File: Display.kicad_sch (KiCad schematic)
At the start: 6 parts, among them J3 Conn_01x30_Pin, U1 rv1126/rv1109

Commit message: updated LCSC selection of capacitors
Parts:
- J3: footprint (none) -> Connector_FFC-FPC:Hirose_FH12-30S-0.5SH_1x30-1MP_P0.50mm_Horizontal
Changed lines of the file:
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@@
       (effects (font (size 1.27 1.27)) (justify right))
     )
-    (property "Footprint" "" (at 226.06 60.96 0)
+    (property "Footprint" "Connector_FFC-FPC:Hirose_FH12-30S-0.5SH_1x30-1MP_P0.50mm_Horizontal" (at 226.06 60.96 0)
       (effects (font (size 1.27 1.27)) hide)
     )

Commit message: layout SoC Power and DDR capacitors
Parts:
- C57: LCSC C76934 -> C76928; Model GRM033R61A104KE15D -> GRM033R60J104KE19D
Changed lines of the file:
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@@
       (effects (font (size 1.27 1.27)) hide)
     )
-    (property "Description" "容值: 100nF 精度: ±10% 额定电压: 10V 材质(温度系数): X5R 材质:X5R" (at 228.6 149.86 0)
-      (effects (font (size 1.27 1.27)) hide)
-    )
-    (property "LCSC" "C76934" (at 228.6 149.86 0)
-      (effects (font (size 1.27 1.27)) hide)
-    )
-    (property "Model" "GRM033R61A104KE15D" (at 228.6 149.86 0)
+    (property "Description" "容值: 100nF 精度: ±10% 额定电压: 6.3V 材质(温度系数): X5R 材质:X5R" (at 228.6 149.86 0)
+      (effects (font (size 1.27 1.27)) hide)
+    )
+    (property "LCSC" "C76928" (at 228.6 149.86 0)
+      (effects (font (size 1.27 1.27)) hide)
+    )
+    (property "Model" "GRM033R60J104KE19D" (at 228.6 149.86 0)
       (effects (font (size 1.27 1.27)) hide)
     )
@@
       (effects (font (size 1.27 1.27)) hide)
     )
-    (property "Description" "容值: 100nF 精度: ±10% 额定电压: 10V 材质(温度系数): X5R 材质:X5R" (at 184.15 148.59 0)
-      (effects (font (size 1.27 1.27)) hide)
-    )
-    (property "LCSC" "C76934" (at 184.15 148.59 0)
-      (effects (font (size 1.27 1.27)) hide)
-    )
-    (property "Model" "GRM033R61A104KE15D" (at 184.15 148.59 0)
-      (effects (font (size 1.27 1.27)) hide)
-    )
+    (property "Description" "容值: 100nF 精度: ±10% 额定电压: 6.3V 材质(温度系数): X5R 材质:X5R" (at 184.15 148.59 0)
+      (effects (font (size 1.27 1.27)) hide)
+    )
+    (property "LCSC" "C76928" (at 184.15 148.59 0)
+      (effects (font (size 1.27 1.27)) hide)
+    )
+    (property "Model" "GRM033R60J104KE19D" (at 184.15 148.59 0)
+      (effects (font (size 1.27 1.27)) hide)
+    )

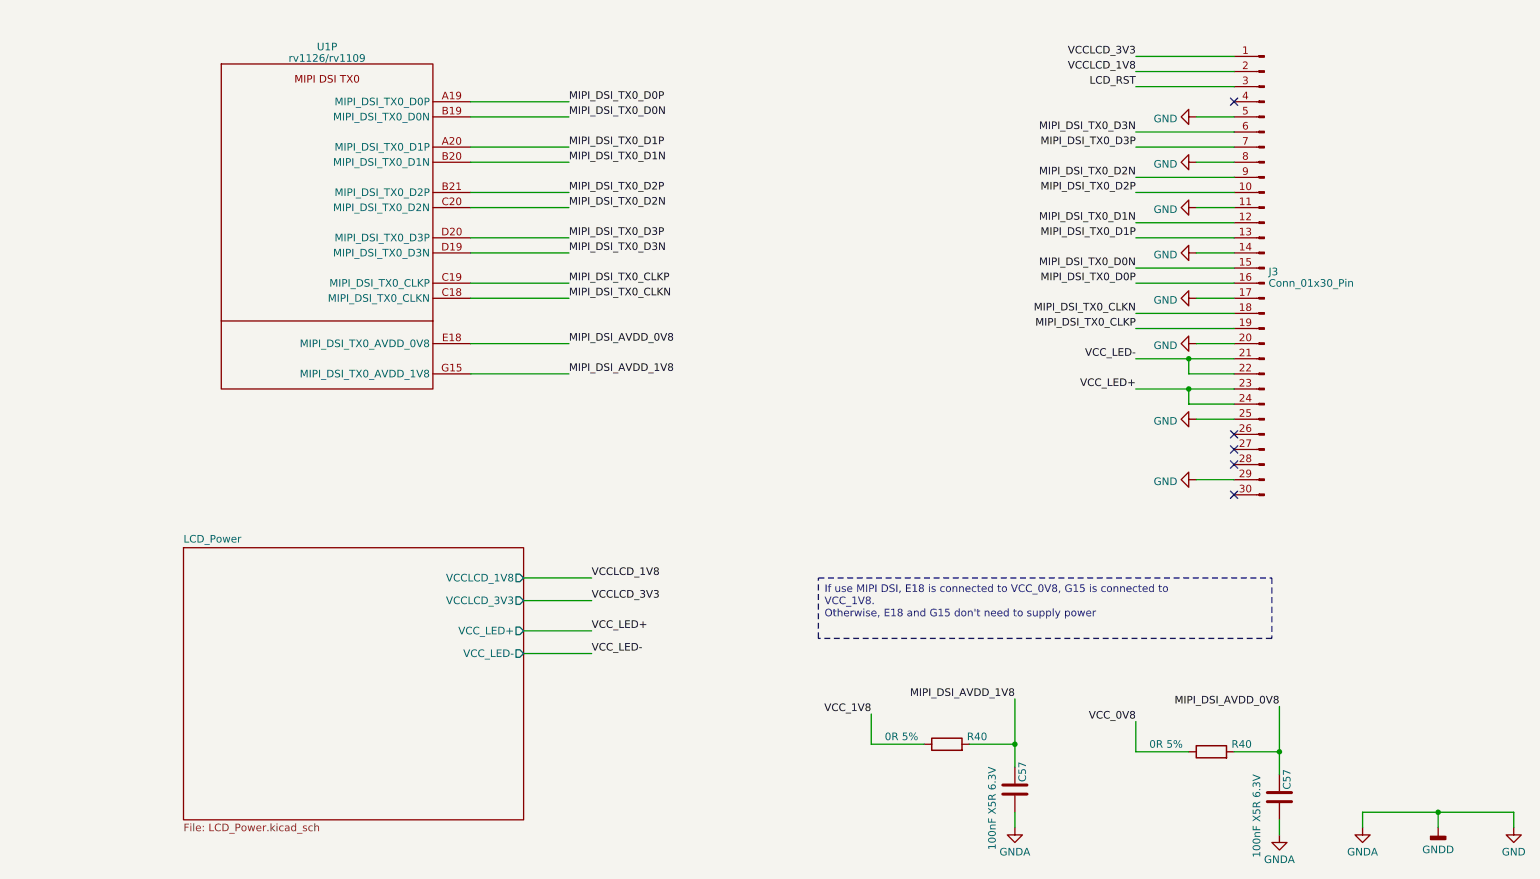
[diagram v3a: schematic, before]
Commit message: fix some ERCs
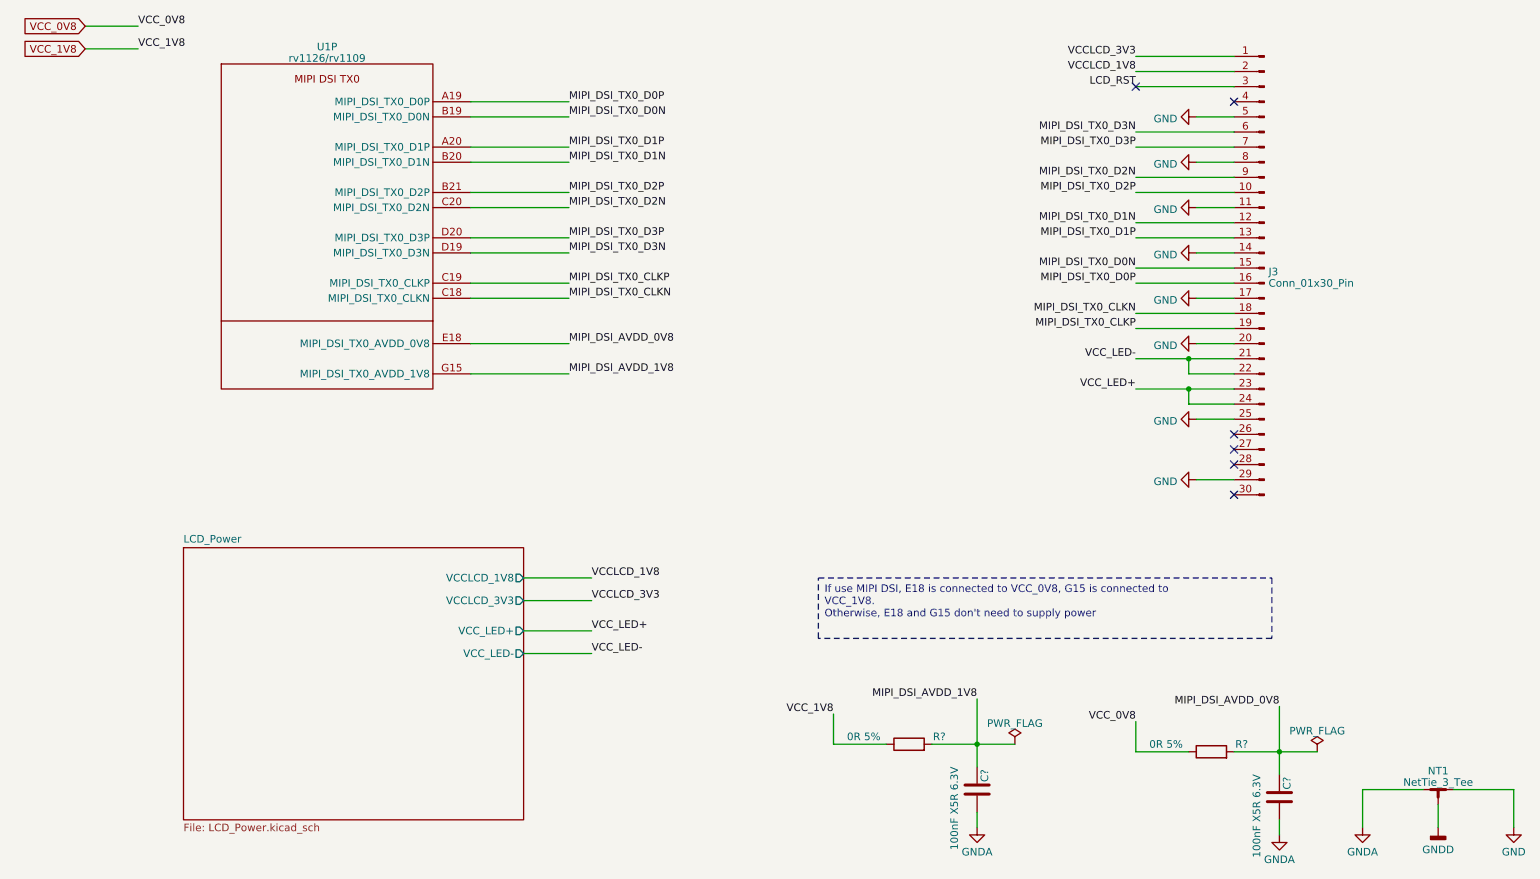
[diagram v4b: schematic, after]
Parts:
- added NT1: NetTie_3_Tee, symbol Device:NetTie_3_Tee
- renumbered C57 to C?, R40 to R?
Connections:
- net GND: now also NT1.2; no longer C?.2, C?.2
- new net GNDA: C?.2, C?.2, NT1.1
- new net GNDD: NT1.3
- no-connect marks 5 -> 6
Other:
- moved on the sheet: C?, R?

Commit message: fix ERC
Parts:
- J3: now not fitted; now left out of the parts list
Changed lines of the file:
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@@
     (pin "E20")
-    (pin "F19")
     (pin "F19")
     (pin "F20")
@@
   )
   (symbol (lib_id "Connector:Conn_01x30_Pin") (at 226.06 60.96 0) (mirror y) (unit 1)
-    (in_bom yes) (on_board yes) (dnp no) (fields_autoplaced)
+    (in_bom no) (on_board no) (dnp yes) (fields_autoplaced)
     (property "Reference" "J3" (at 226.7712 61.5863 0)
       (effects (font (size 1.27 1.27)) (justify right))

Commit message: updated symbols
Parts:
- removed C? (x2): 100nF X5R 6.3V, Capacitor_SMD:C_0201_0603Metric, symbol Device:C
- removed J3: Conn_01x30_Pin, Connector_FFC-FPC:Hirose_FH12-30S-0.5SH_1x30-1MP_P0.50mm_Horizontal, symbol Connector:Conn_01x30_Pin
- removed NT1: NetTie_3_Tee, symbol Device:NetTie_3_Tee
- removed R? (x2): 0R 5%, Resistor_SMD:R_0402_1005Metric, symbol Device:R
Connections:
- no-connect marks 6 -> 12
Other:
- removed sheet LCD_Power

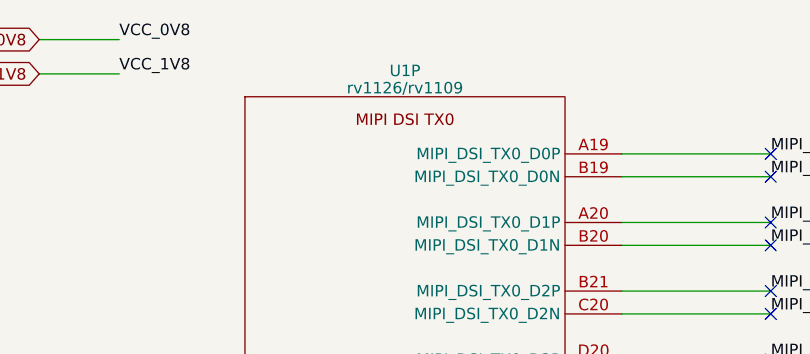
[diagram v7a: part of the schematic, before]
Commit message: added OSC, updated annotations
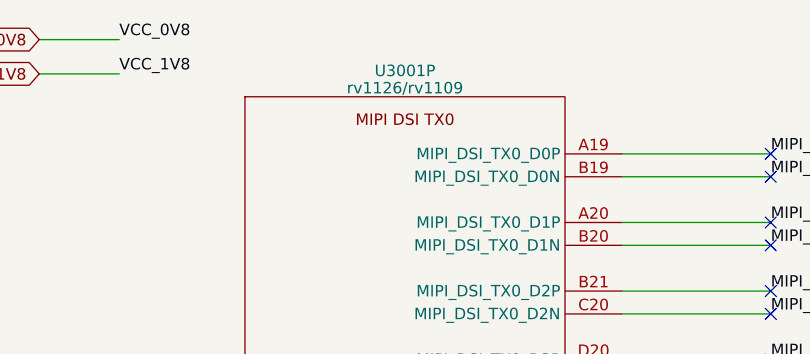
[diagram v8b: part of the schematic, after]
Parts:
- renumbered U1 to U3001
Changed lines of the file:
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@@
   (symbol (lib_id "CPU_Rockchip:rv1126_rv1109") (at 68.58 57.15 0) (unit 16)
     (in_bom yes) (on_board yes) (dnp no) (fields_autoplaced)
-    (property "Reference" "U1" (at 68.58 23.7871 0)
+    (property "Reference" "U3001" (at 68.58 23.7871 0)
       (effects (font (size 1.27 1.27)))
     )
@@
       (project "leaf"
         (path "/e3b58043-16a3-43c8-9fad-9c9784eebfa4/abba4c44-e9bc-404f-bbc8-3409461eb15e"
-          (reference "U1") (unit 16)
+          (reference "U3001") (unit 16)
         )
       )
